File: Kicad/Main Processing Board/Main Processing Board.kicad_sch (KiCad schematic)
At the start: 2 parts, among them J1 MEM2061-01-188-00-A_REVA, U1 Seeed Studio XIAO RA4M1

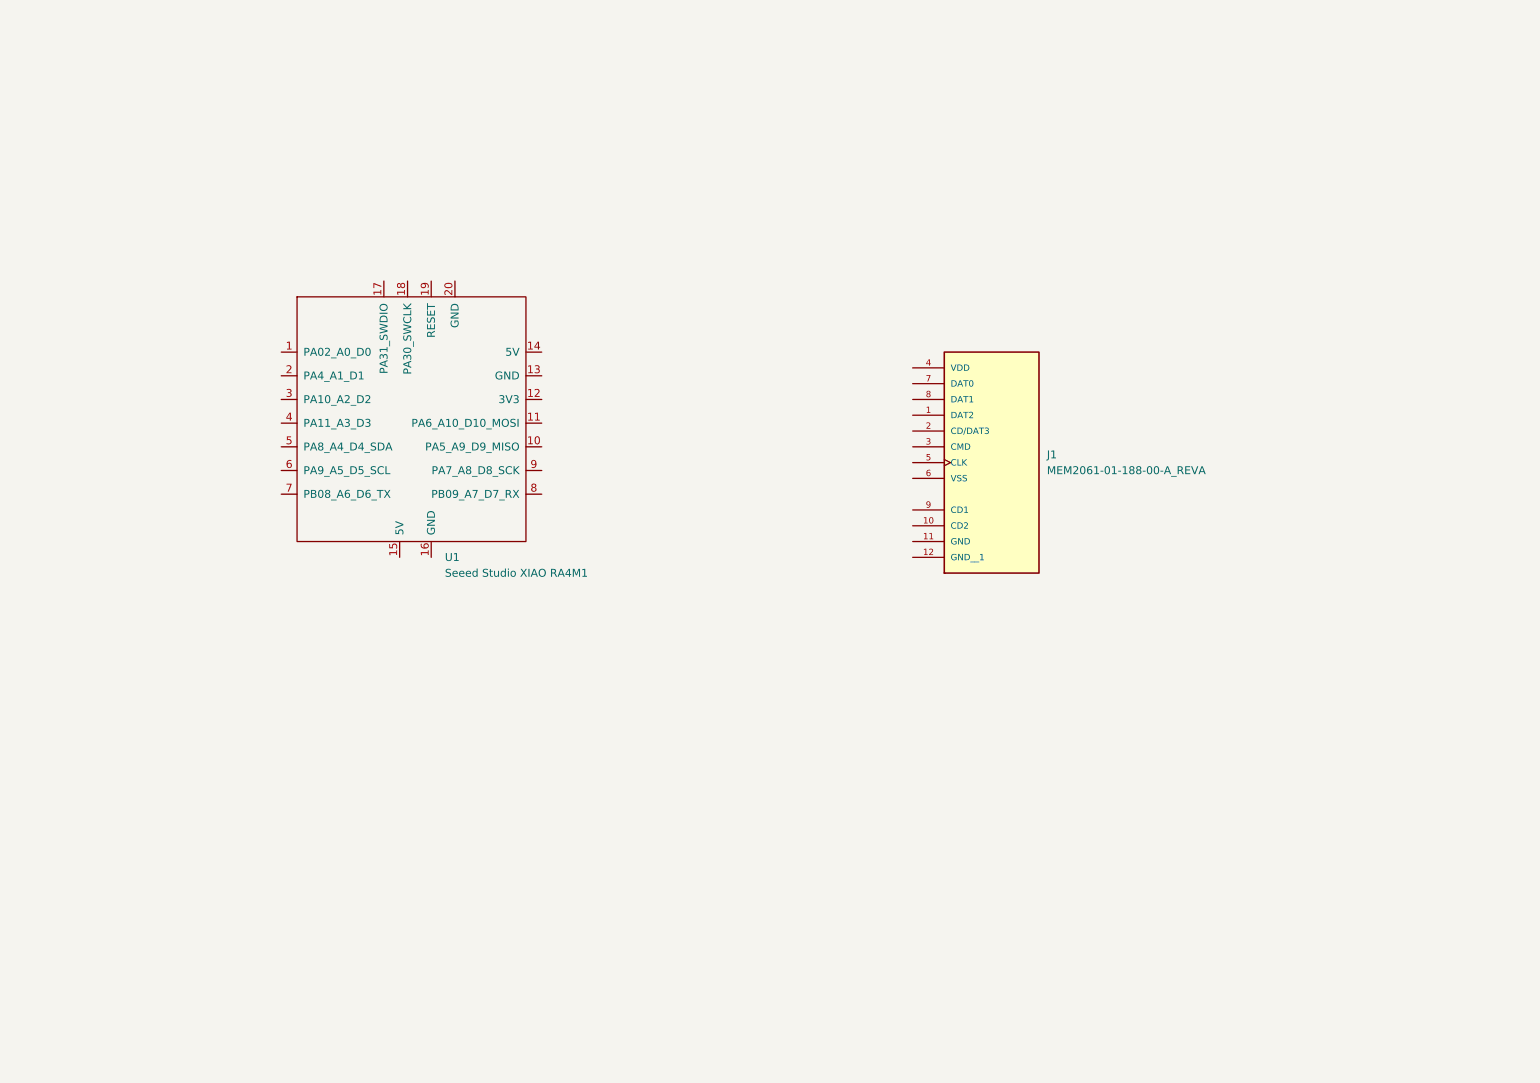
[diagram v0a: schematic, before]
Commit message: Wired SD card and Camera
- Made new schematic for RA4M1
- Made I2C and SPI labels
- Started wiring
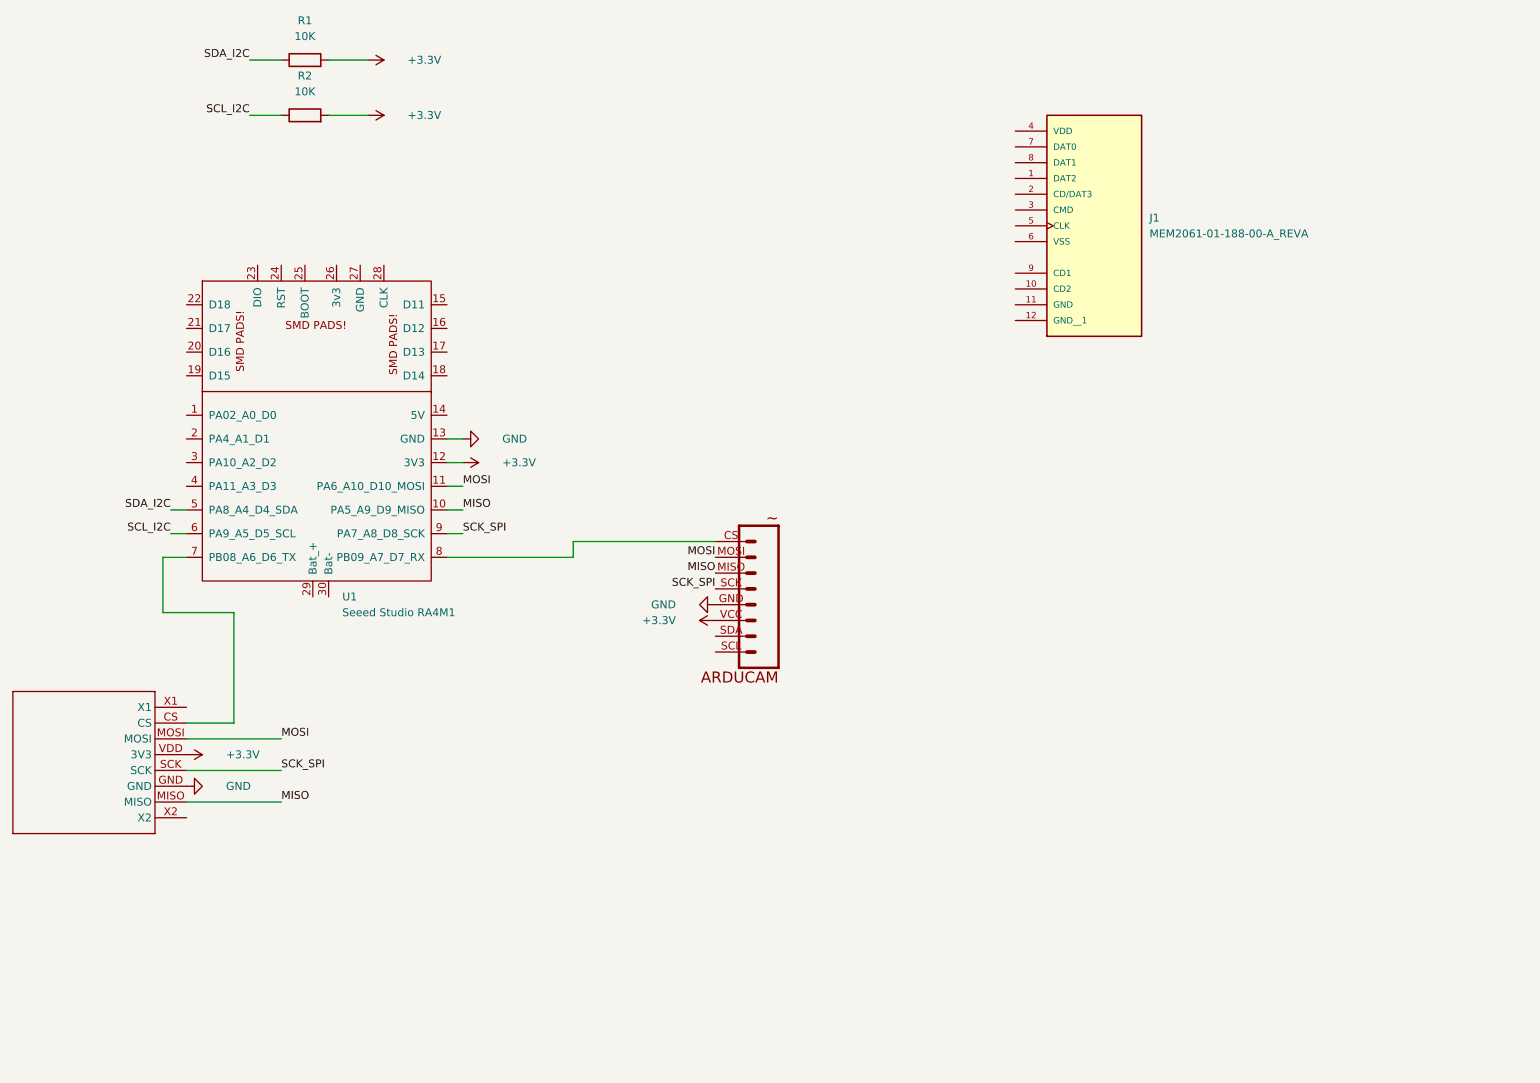
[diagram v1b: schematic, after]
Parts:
- removed U1: Seeed Studio XIAO RA4M1, Seeed Studio XIAO Series Library:XIAO-RP2040-SMD, symbol Seeed_Studio_XIAO_Series:Seeed Studio XIAO SAMD21
- added 1: ~, project-library:ARDUCAM_MINI, symbol project-library:ARDUCAM_MINI
- added 1: ~, project-library:SDREAD, symbol project-library:SD_READER
- added R1, R2: 10K, symbol Device:R
- added U1: Seeed Studio RA4M1, symbol Pocket Qube Symbols:Seeed Studio RA4M1
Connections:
- new net: 1.CS, U1.8 (PB09_A7_D7_RX)
- new net: 1.CS, U1.7 (PB08_A6_D6_TX)
- new net +3.3V: 1.VCC, 1.VDD (3V3), R1.2, R2.2, U1.12 (3V3)
- new net GND: 1.GND, 1.GND, U1.13 (GND)
- new net MISO: 1.MISO, 1.MISO, U1.10 (PA5_A9_D9_MISO)
- new net MOSI: 1.MOSI, 1.MOSI, U1.11 (PA6_A10_D10_MOSI)
- new net SCK_SPI: 1.SCK, 1.SCK, U1.9 (PA7_A8_D8_SCK)
- new net SCL_I2C: R2.1, U1.6 (PA9_A5_D5_SCL)
- new net SDA_I2C: R1.1, U1.5 (PA8_A4_D4_SDA)
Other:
- moved on the sheet: J1

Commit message: added basis for main system
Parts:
- renumbered 1 to 11, 1 to 12
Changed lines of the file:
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@@
 		(dnp no)
 		(fields_autoplaced yes)
-		(property "Reference" "1"
+		(property "Reference" "12"
 			(at 173.99 111.76 0)
 			(effects
@@
 			(project ""
 				(path "/3370e2f3-9ba2-43e2-b682-b04be93477ce"
-					(reference "1")
+					(reference "12")
 					(unit 1)
 				)
@@
 		(dnp no)
 		(fields_autoplaced yes)
-		(property "Reference" "1"
+		(property "Reference" "11"
 			(at 66.04 140.97 0)
 			(effects
@@
 			(project ""
 				(path "/3370e2f3-9ba2-43e2-b682-b04be93477ce"
-					(reference "1")
+					(reference "11")
 					(unit 1)
 				)

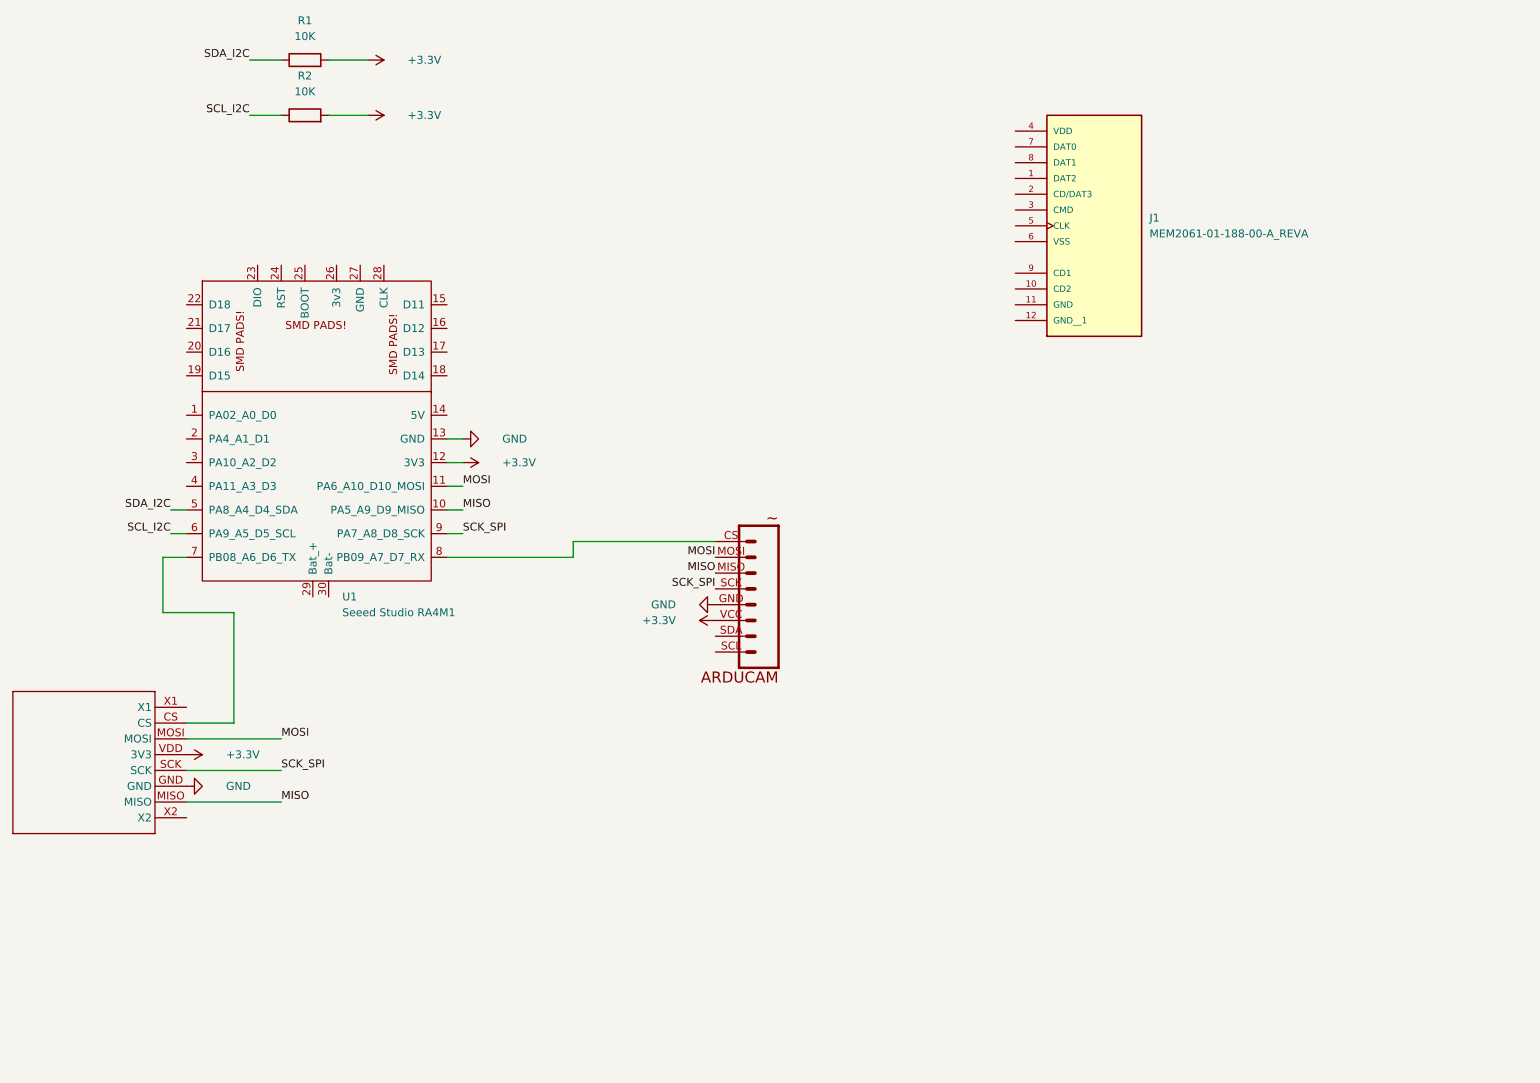
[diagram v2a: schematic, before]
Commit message: added dataLogger structure
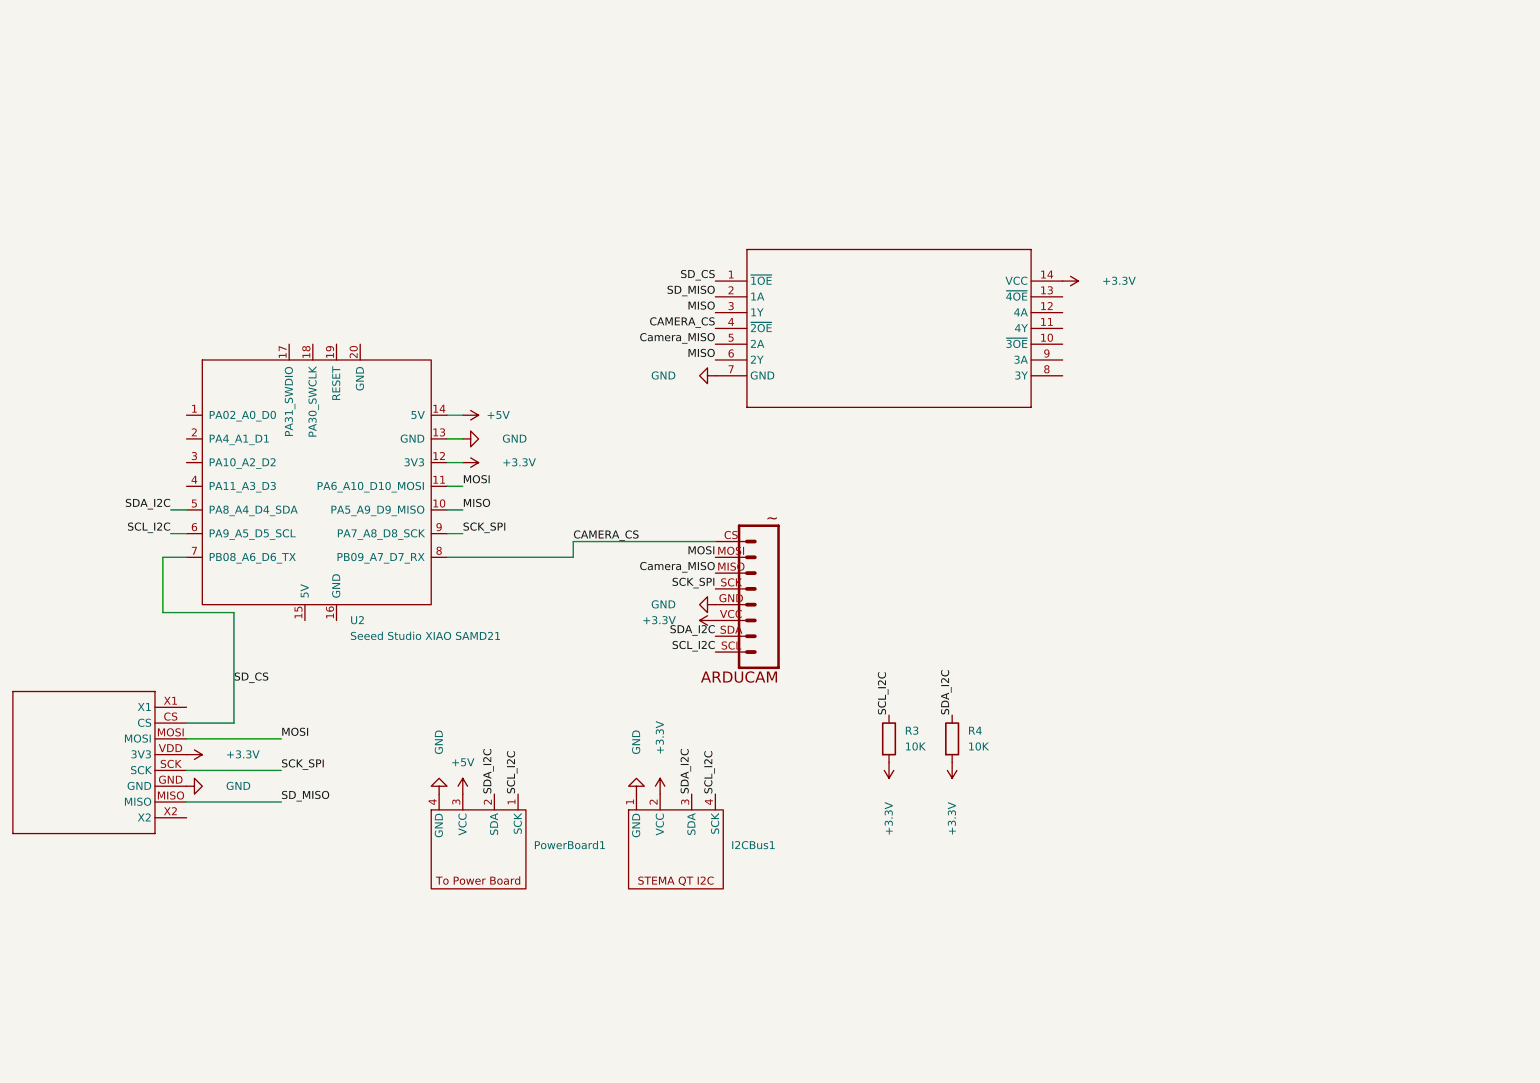
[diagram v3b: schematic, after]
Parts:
- removed J1: MEM2061-01-188-00-A_REVA, MEM2061_01_188_00_A:GCT_MEM2061-01-188-00-A_REVA, symbol MEM2061-01-188-00-A_REVA:MEM2061-01-188-00-A_REVA
- removed R1, R2: 10K, symbol Device:R
- removed U1: Seeed Studio RA4M1, symbol Pocket Qube Symbols:Seeed Studio RA4M1
- added I2CBus1: ~, Connector_JST:JST_SH_BM04B-SRSS-TB_1x04-1MP_P1.00mm_Vertical, symbol Pocket Qube Symbols:Stema_QT
- added PowerBoard1: ~, Connector_Molex:Molex_PicoBlade_53047-0410_1x04_P1.25mm_Vertical, symbol Pocket Qube Symbols:I2C_Power_Connector
- added R3, R4: 10K, symbol Device:R
- added U1: ~, SN74LVC125ANSR:NS14, symbol SN74LVC125ANSR:SN74LVC125ANSR
- added U2: Seeed Studio XIAO SAMD21, Seeed Studio XIAO Series Library:XIAO-SAMD21-SMD, symbol Seeed_Studio_XIAO_Series:Seeed Studio XIAO SAMD21
- renumbered 11 to 111, 12 to 121
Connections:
- net +3.3V: now also I2CBus1.2 (VCC), R3.2, R4.2, U1.14 (VCC), U2.12 (3V3)
- net GND: now also I2CBus1.1 (GND), PowerBoard1.4 (GND), U1.7 (GND), U2.13 (GND)
- net MISO: now also U1.3 (1Y), U1.6 (2Y), U2.10 (PA5_A9_D9_MISO); no longer 111.MISO, 121.MISO
- net MOSI: now also U2.11 (PA6_A10_D10_MOSI)
- net SCK_SPI: now also U2.9 (PA7_A8_D8_SCK)
- net SCL_I2C: now also 121.SCL, I2CBus1.4 (SCK), PowerBoard1.1 (SCK), R3.1, U2.6 (PA9_A5_D5_SCL)
- net SDA_I2C: now also 121.SDA, I2CBus1.3 (SDA), PowerBoard1.2 (SDA), R4.1, U2.5 (PA8_A4_D4_SDA)
- net CAMERA_CS: now reaches 121.CS
- net CAMERA_CS: now also U1.4 (~{2OE}), U2.8 (PB09_A7_D7_RX)
- net SD_CS: now reaches 111.CS
- net SD_CS: now also U1.1 (~{1OE}), U2.7 (PB08_A6_D6_TX)
- new net +5V: PowerBoard1.3 (VCC), U2.14 (5V)
- new net Camera_MISO: 121.MISO, U1.5 (2A)
- new net SD_MISO: 111.MISO, U1.2 (1A)

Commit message: more work on kicad
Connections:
- net MISO: now also U1.11 (4Y)
- net Radio_Reset: now reaches U2.2 (PA4_A1_D1)
- net Radio_G0: now reaches U2.3 (PA10_A2_D2)
- net Radio_CS: now reaches U2.4 (PA11_A3_D3)
- net Radio_CS: now also U1.13 (~{4OE})
- net Radio_MISO: now reaches U1.12 (4A)
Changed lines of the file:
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@@
+		)
+	)
+	(label "Radio_CS"
+		(at 83.82 95.25 180)
+		(fields_autoplaced yes)
+		(effects
+			(font
+				(size 1.27 1.27)
+			)
+			(justify right bottom)
 		)
 	)
@@
 		)
 	)
+	(label "Radio_G0"
+		(at 83.82 91.44 180)
+		(fields_autoplaced yes)
+		(effects
+			(font
+				(size 1.27 1.27)
+			)
+			(justify right bottom)
+		)
+	)
 	(label "SDA_I2C"
 		(at 165.1 144.78 90)
+		(fields_autoplaced yes)
+		(effects
+			(font
+				(size 1.27 1.27)
+			)
+			(justify left bottom)
+		)
+	)
+	(label "Radio_MISO"
+		(at 224.79 67.31 0)
 		(fields_autoplaced yes)
 		(effects
@@
 		)
 	)
+	(label "Radio_Reset"
+		(at 83.82 87.63 180)
+		(fields_autoplaced yes)
+		(effects
+			(font
+				(size 1.27 1.27)
+			)
+			(justify right bottom)
+		)
+	)
 	(label "SDA_I2C"
 		(at 168.91 119.38 180)
@@
 		)
 	)
+	(label "Radio_CS"
+		(at 224.79 64.77 0)
+		(fields_autoplaced yes)
+		(effects
+			(font
+				(size 1.27 1.27)
+			)
+			(justify left bottom)
+		)
+	)
 	(label "MOSI"
 		(at 128.27 95.25 0)
@@
 		(fields_autoplaced yes)
 		(effects
+			(font
+				(size 1.27 1.27)
+			)
+			(justify left bottom)
+		)
+	)
+	(label "MISO"
+		(at 224.79 69.85 0)
+		(fields_autoplaced yes)
+		(effects

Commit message: updates to pcb and code
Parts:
- added AtmosphericCapacitor1: 100nF, symbol Device:C
- added AtmosphericSensor1: MS5611-01BA03, MS5611:SON125P500X300X100-8N, symbol MS5611-01BA03:MS5611-01BA03
- renumbered 111 to 11111, 121 to 12111
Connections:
- net +3.3V: now also AtmosphericCapacitor1.1, AtmosphericSensor1.1 (VDD), AtmosphericSensor1.2 (PS), AtmosphericSensor1.4 (CSB), AtmosphericSensor1.5 (CSB)
- net GND: now also AtmosphericCapacitor1.2, AtmosphericSensor1.3 (GND)
- net SCL_I2C: now also AtmosphericSensor1.8 (SCLK)
- net SDA_I2C: now also AtmosphericSensor1.7 (SDI/SDA)

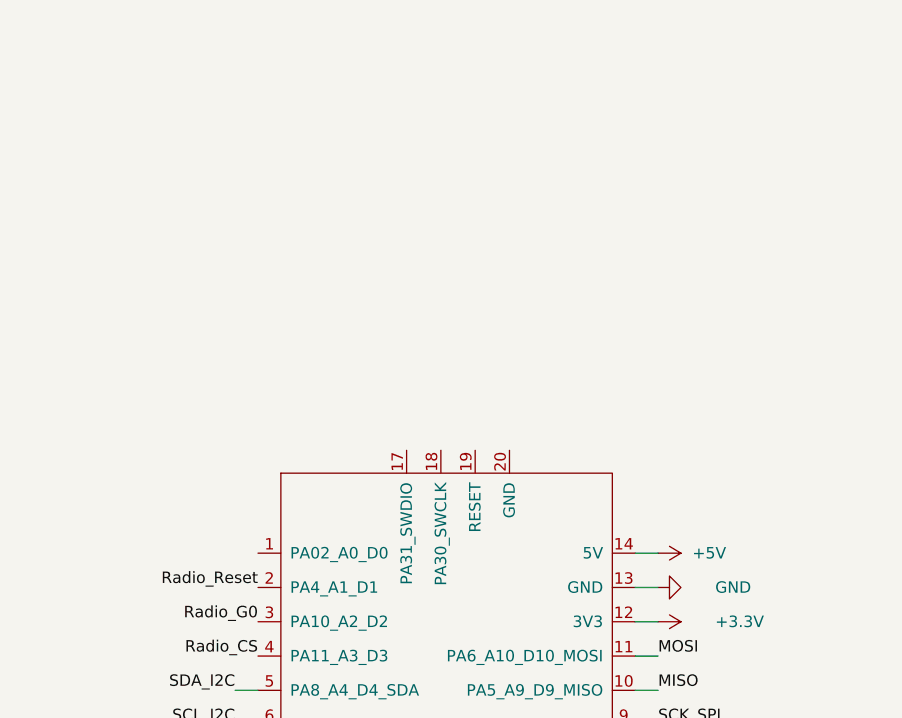
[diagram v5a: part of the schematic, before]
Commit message: added 3d models
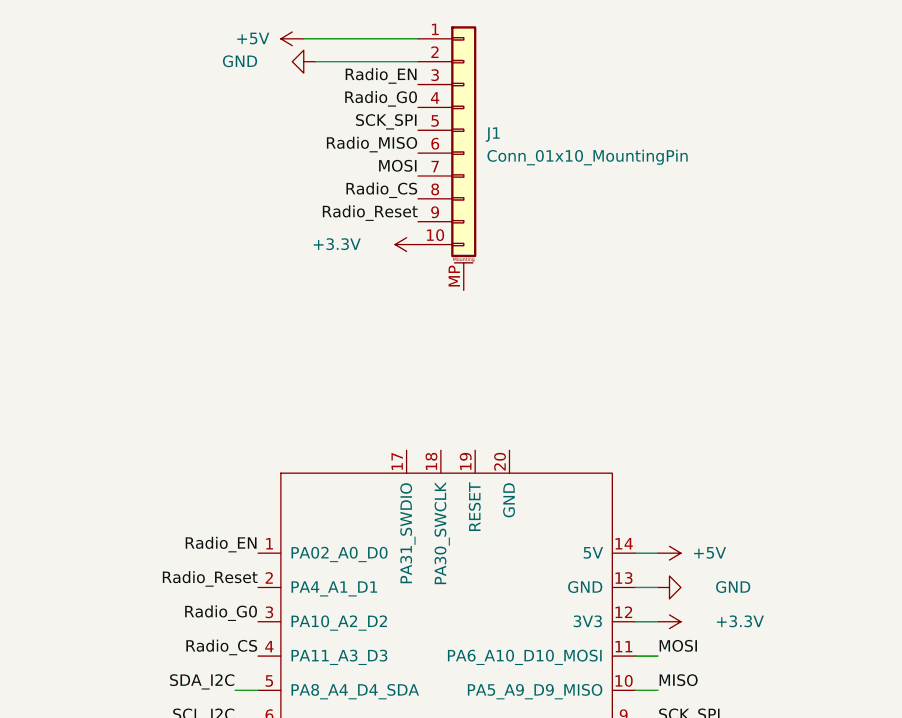
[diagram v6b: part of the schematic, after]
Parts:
- added J1: Conn_01x10_MountingPin, Connector_JST:JST_SH_BM10B-SRSS-TB_1x10-1MP_P1.00mm_Vertical, symbol Connector_Generic_MountingPin:Conn_01x10_MountingPin
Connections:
- net +3.3V: now also J1.10 (Pin_10)
- net +5V: now also J1.1 (Pin_1)
- net GND: now also J1.2 (Pin_2)
- net MOSI: now also J1.7 (Pin_7)
- net Radio_CS: now also J1.8 (Pin_8)
- net Radio_G0: now also J1.4 (Pin_4)
- net Radio_MISO: now also J1.6 (Pin_6)
- net Radio_Reset: now also J1.9 (Pin_9)
- net SCK_SPI: now also J1.5 (Pin_5)
- net Radio_EN: now reaches U2.1 (PA02_A0_D0)
- net Radio_EN: now also J1.3 (Pin_3)
